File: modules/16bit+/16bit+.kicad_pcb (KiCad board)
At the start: 2 copper layers, 30.5 x 68.6 mm, 51 parts, among them J1 Conn_01x08_Socket, J2 Conn_01x08_Socket, J5 USB_C_Receptacle_USB2.0_14P, SW1 K2-1808SN-A4SW-01, SW2 K2-1808SN-A4SW-01, SW3 K2-1808SN-A4SW-01, U1 RP2350_60QFN, U2 W25Q128JVS, U3 MCP6002-xSN, U5 PSRAM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

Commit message: Detect 16bit+ at runtime via IO21
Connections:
- U1 pad 33: unconnected-(U1-GPIO21-Pad33) -> GND
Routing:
- net GND: track 76.0 -> 77.0 mm, vias 31 -> 32

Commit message: Finalize the schematics
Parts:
- added C21: 0.1uf, Capacitor_SMD:C_0402_1005Metric, F.Cu at (92.3, 65.1)
- added C22: 0.1uf, Capacitor_SMD:C_0402_1005Metric, F.Cu at (92.3, 67.1)
- added C23: 1uf, Capacitor_SMD:C_0402_1005Metric, F.Cu at (92.3, 69.1)
- added C25: 1uf, Capacitor_SMD:C_0402_1005Metric, F.Cu at (95.2, 63.1)
- added C26: 0.1uf, Capacitor_SMD:C_0402_1005Metric, F.Cu at (95.2, 65.1)
- added C27: 10uf, Capacitor_SMD:C_0402_1005Metric, F.Cu at (95.2, 67.1)
- added C30: 1uf, Capacitor_SMD:C_0402_1005Metric, F.Cu at (95.2, 69.1)
- added C31: 1uf, Capacitor_SMD:C_0402_1005Metric, F.Cu at (98.0, 63.1)
- added C33: 10uf, Capacitor_SMD:C_0402_1005Metric, F.Cu at (98.0, 65.1)
- added C34: 0.1uf, Capacitor_SMD:C_0402_1005Metric, F.Cu at (98.0, 67.1)
- added C35: 10uf, Capacitor_SMD:C_0402_1005Metric, F.Cu at (98.0, 69.1)
- added C36: 0.1uf, Capacitor_SMD:C_0402_1005Metric, F.Cu at (100.9, 63.1)
- added C37: 10uf, Capacitor_SMD:C_0402_1005Metric, F.Cu at (100.9, 65.1)
- added C38: 10uf, Capacitor_SMD:C_0402_1005Metric, F.Cu at (100.9, 67.1)
- added C39: 0.1uf, Capacitor_SMD:C_0402_1005Metric, F.Cu at (100.9, 69.1)
- added C5: 10uf, Capacitor_SMD:C_0402_1005Metric, F.Cu at (92.3, 63.1)
- added R13: 1k, Resistor_SMD:R_0402_1005Metric, F.Cu at (98.6, 71.0)
- added R17: 1k, Resistor_SMD:R_0402_1005Metric, F.Cu at (98.6, 77.0)
- added R19: 33, Resistor_SMD:R_0402_1005Metric, F.Cu at (98.6, 79.0)
- added R20: 33, Resistor_SMD:R_0402_1005Metric, F.Cu at (98.6, 81.0)
- added R21: 33, Resistor_SMD:R_0402_1005Metric, F.Cu at (101.5, 71.0)
- added R22: 33, Resistor_SMD:R_0402_1005Metric, F.Cu at (101.5, 73.0)
- added R23: 33, Resistor_SMD:R_0402_1005Metric, F.Cu at (101.5, 75.0)
- added R24: 10k, Resistor_SMD:R_0402_1005Metric, F.Cu at (101.5, 77.0)
- added R25: 10k, Resistor_SMD:R_0402_1005Metric, F.Cu at (101.5, 79.0)
- added U4: ~, Package_DFN_QFN:QFN-28-1EP_4x4mm_P0.45mm_EP2.4x2.4mm_ThermalVias, F.Cu at (71.0, 101.0)
- moved R16 49.4 mm to (98.6, 75.0)
- moved R15 49.3 mm to (98.6, 73.0), turned to 0 degrees
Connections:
- R15 pad 1: AIN_2 -> AIN_1
- R16 pad 1: GND -> AIN_2
- R16 pad 2: AIN_1 -> GND
- U1 pad 10: unconnected-(U1-GPIO7-Pad10) -> SCLK
- U1 pad 12: unconnected-(U1-GPIO8-Pad12) -> DSDIN
- U1 pad 13: unconnected-(U1-GPIO9-Pad13) -> LRCK
- U1 pad 14: unconnected-(U1-GPIO10-Pad14) -> ASDOUT
- U1 pad 4: unconnected-(U1-GPIO2-Pad4) -> CDATA
- U1 pad 40: AIN_1 -> unconnected-(U1-GPIO26_ADC0-Pad40)
- U1 pad 41: AIN_2 -> unconnected-(U1-GPIO27_ADC1-Pad41)
- U1 pad 5: unconnected-(U1-GPIO3-Pad5) -> CCLK
- U1 pad 9: unconnected-(U1-GPIO6-Pad9) -> MCLK
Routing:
- net AIN_1: track 50.4 -> 0.00 mm, vias 3 -> 0
- net AIN_2: track 46.2 -> 0.00 mm, vias 3 -> 0
- net GND: track 77.0 -> 74.6 mm, vias 32 -> 31

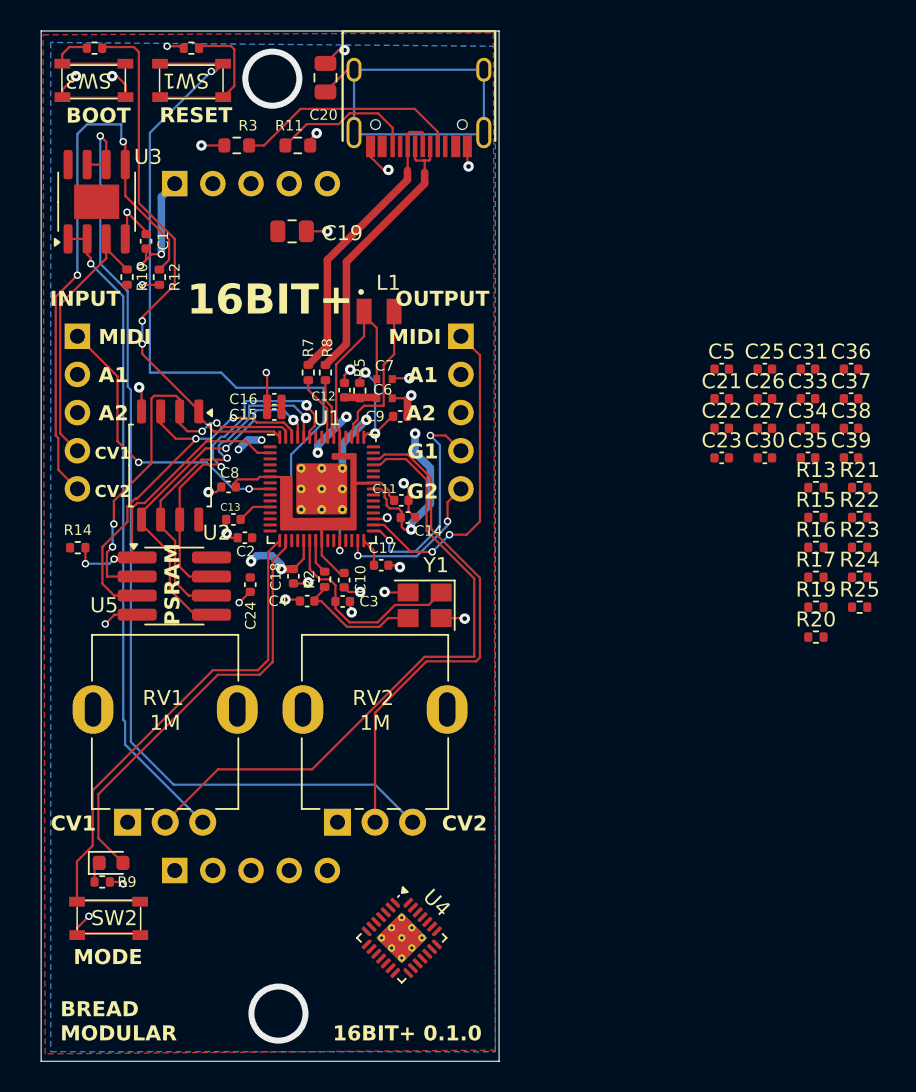
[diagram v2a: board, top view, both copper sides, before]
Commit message: finalize audio codec routing
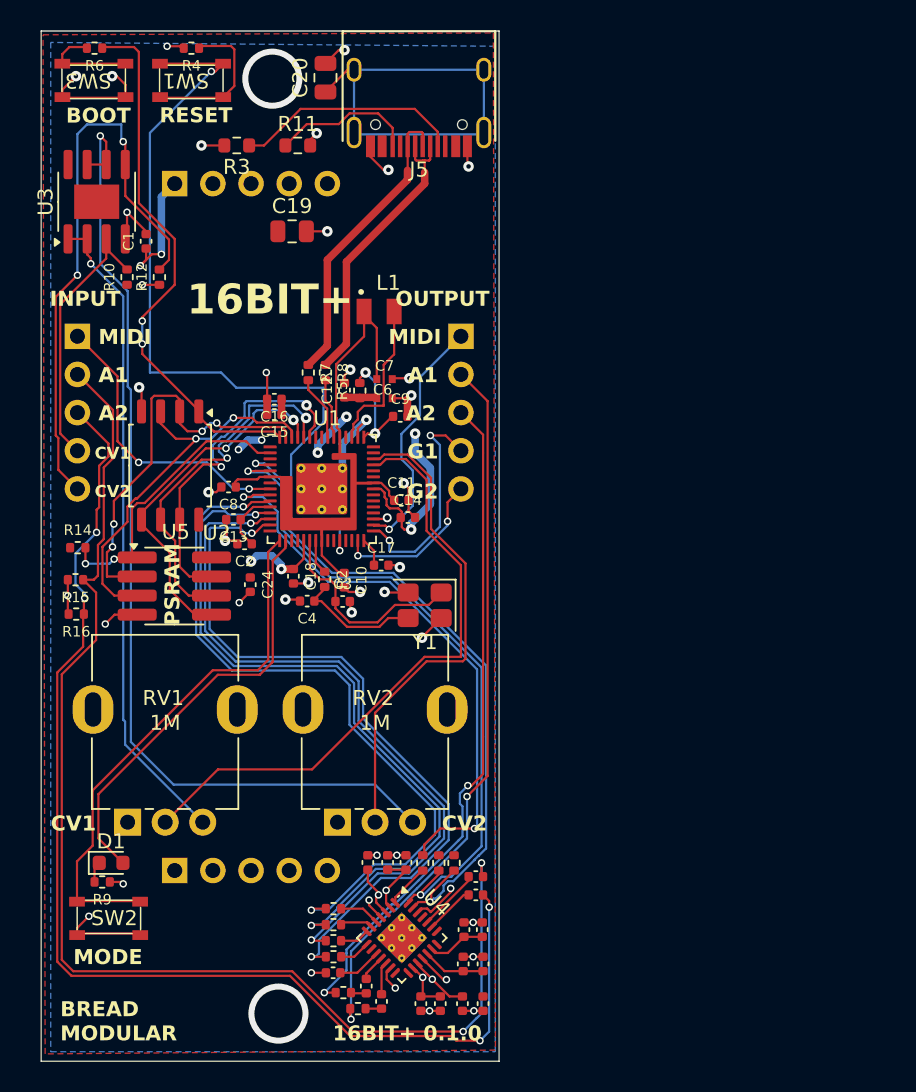
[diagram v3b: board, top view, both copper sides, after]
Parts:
- moved R15 49.5 mm to (49.3, 77.2), turned to 180 degrees
- moved R16 49.4 mm to (49.3, 79.5), turned to 180 degrees
- moved C25 49.2 mm to (69.6, 105.2), turned to 90 degrees
- moved C37 47.9 mm to (75.0, 105.4), turned to -90 degrees
- moved C38 47.8 mm to (72.3, 105.4), turned to -90 degrees
- moved C36 46.6 mm to (76.4, 102.7), turned to 90 degrees
- moved C27 46.3 mm to (66.4, 103.3)
- moved R13 46.0 mm to (67.1, 104.6)
- moved R21 45.5 mm to (66.4, 100.1)
- moved C39 45.5 mm to (73.6, 105.4), turned to -90 degrees
- moved R22 44.9 mm to (66.4, 101.2)
- moved C26 44.4 mm to (76.4, 105.4), turned to -90 degrees
- moved R23 44.4 mm to (66.4, 102.3)
- moved C23 42.4 mm to (68.6, 104.2), turned to 90 degrees
- moved C33 42.1 mm to (75.1, 100.5), turned to 90 degrees
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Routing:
- net AIN_1: track 0.00 -> 84.0 mm, vias 0 -> 2
- net AIN_2: track 0.00 -> 79.8 mm, vias 0 -> 4
- net ASDOUT: track 0.00 -> 49.6 mm, vias 0 -> 2
- net DSDIN: track 0.00 -> 48.6 mm, vias 0 -> 2
- net LRCK: track 0.00 -> 48.6 mm, vias 0 -> 2
- net AOUT_1: track 0.00 -> 48.3 mm, vias 0 -> 2
- net SCLK: track 0.00 -> 48.2 mm, vias 0 -> 2
- net CDATA: track 0.00 -> 45.2 mm, vias 0 -> 2
- net AOUT_2: track 0.00 -> 44.8 mm, vias 0 -> 2
- net CCLK: track 0.00 -> 44.6 mm, vias 0 -> 2
- net MCLK: track 0.00 -> 38.0 mm, vias 0 -> 2
- net GND: track 74.6 -> 93.6 mm, vias 31 -> 43
- net +3V3: track 39.7 -> 56.9 mm, vias 11 -> 15
- net MIDI_OUT: track 21.5 -> 16.6 mm, vias 2 -> 1
- net Net-(U4-ADCVREF): track 0.00 -> 4.19 mm
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
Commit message: Finalize all the routing
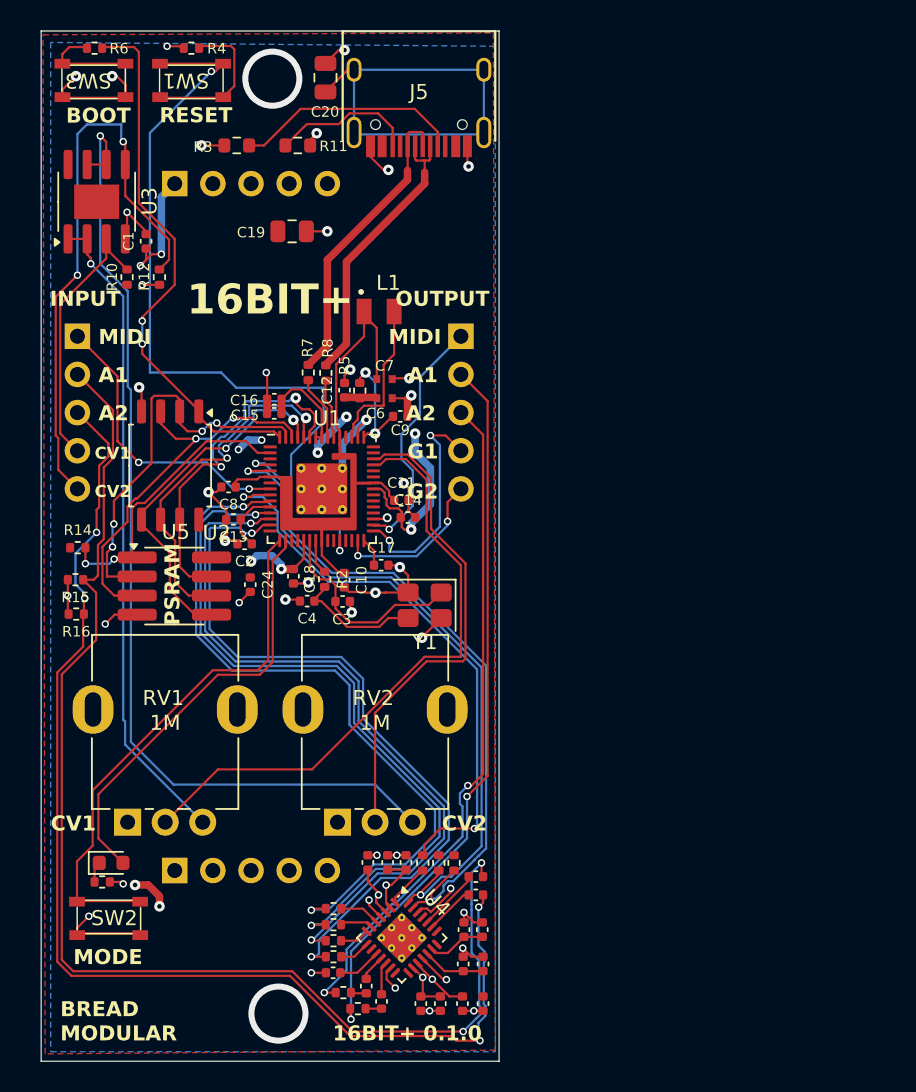
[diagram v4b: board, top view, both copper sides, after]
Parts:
- moved C15 0.08 mm to (62.5, 66.1)
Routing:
- net +3V3: track 56.9 -> 65.9 mm, vias 15 -> 17
- net GND: track 93.6 -> 101.3 mm, vias 43 -> 42
- net AIN_1: track 84.0 -> 84.5 mm
